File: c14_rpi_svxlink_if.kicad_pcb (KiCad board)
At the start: 2 copper layers, 87 x 56 mm, 52 parts, among them J1 RPi_GPIO, J2 Conn_01x04, J3 Conn_01x04, J4 Conn_01x04, J5 Conn_01x02, J6 Conn_01x04, J7 DB9F, Q1 BC847, Q2 BC847, Q3 BC847, Q4 BC857, T1 1:1, T2 1:1, U1 TLP222A, U2 HCPL-B17, U3 ADS1115_Module

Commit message: Small preproduction changes
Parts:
- C3: footprint Capacitor_THT:C_Rect_L7.2mm_W3.5mm_P5.00mm_FKS2_FKP2_MKS2_MKP2 -> Capacitor_THT:C_Rect_L7.2mm_W4.5mm_P5.00mm_FKS2_FKP2_MKS2_MKP2
- D3: value 18V -> TVS 18V
- J1: value RPi_GPIO -> RPi_GPIO Tall
- U1: value TLP222A -> TLP222A o. AQY282EH
- moved R18 16.9 mm to (198.8, 91.1)
- moved C6 16.8 mm to (196.1, 91.0)
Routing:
- net /RSSI: track 34.8 -> 17.7 mm
- net Net-(C6-Pad2): track 6.03 -> 16.4 mm
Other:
- board text added: "DL1COM C14 RPI SVXLINK IF v1.0"
- board text removed: "C14 RPI SVXLINK IF v1.0"

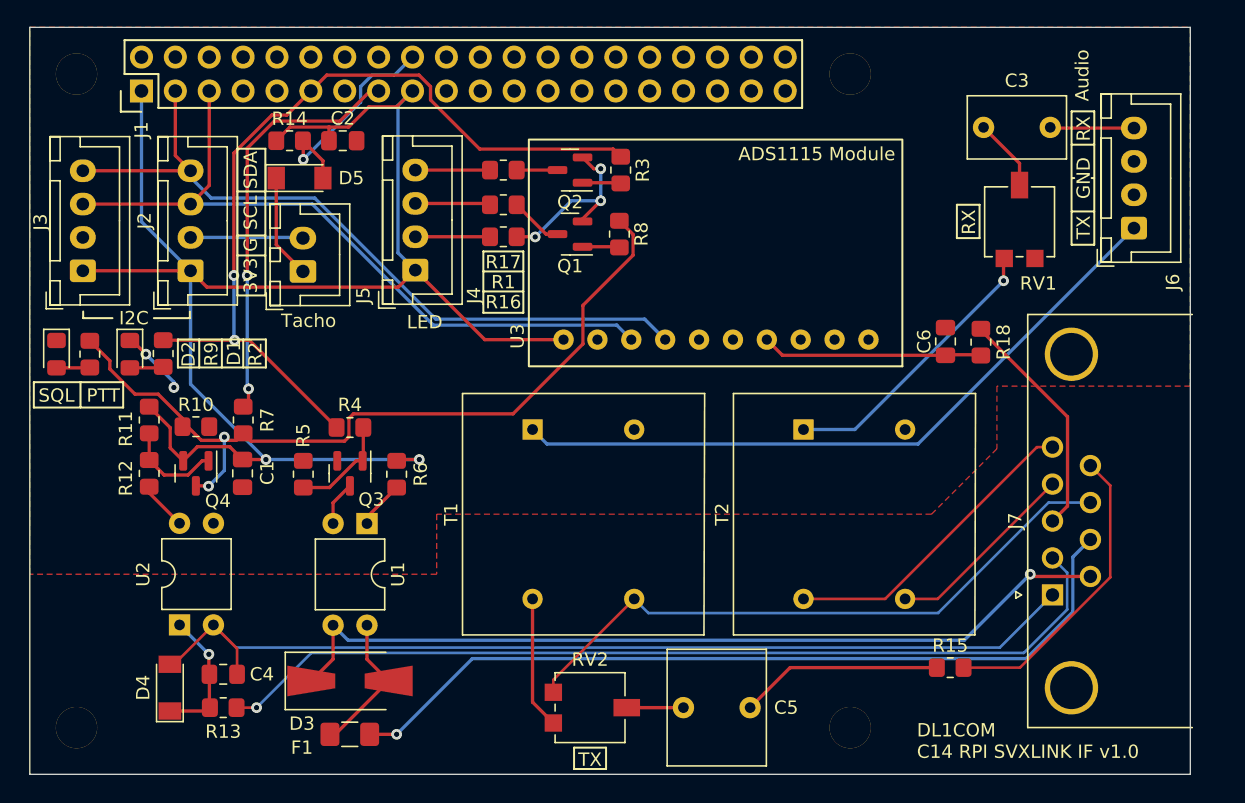
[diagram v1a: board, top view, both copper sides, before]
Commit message: Fix: Correct Footprint for J7 (M->F)
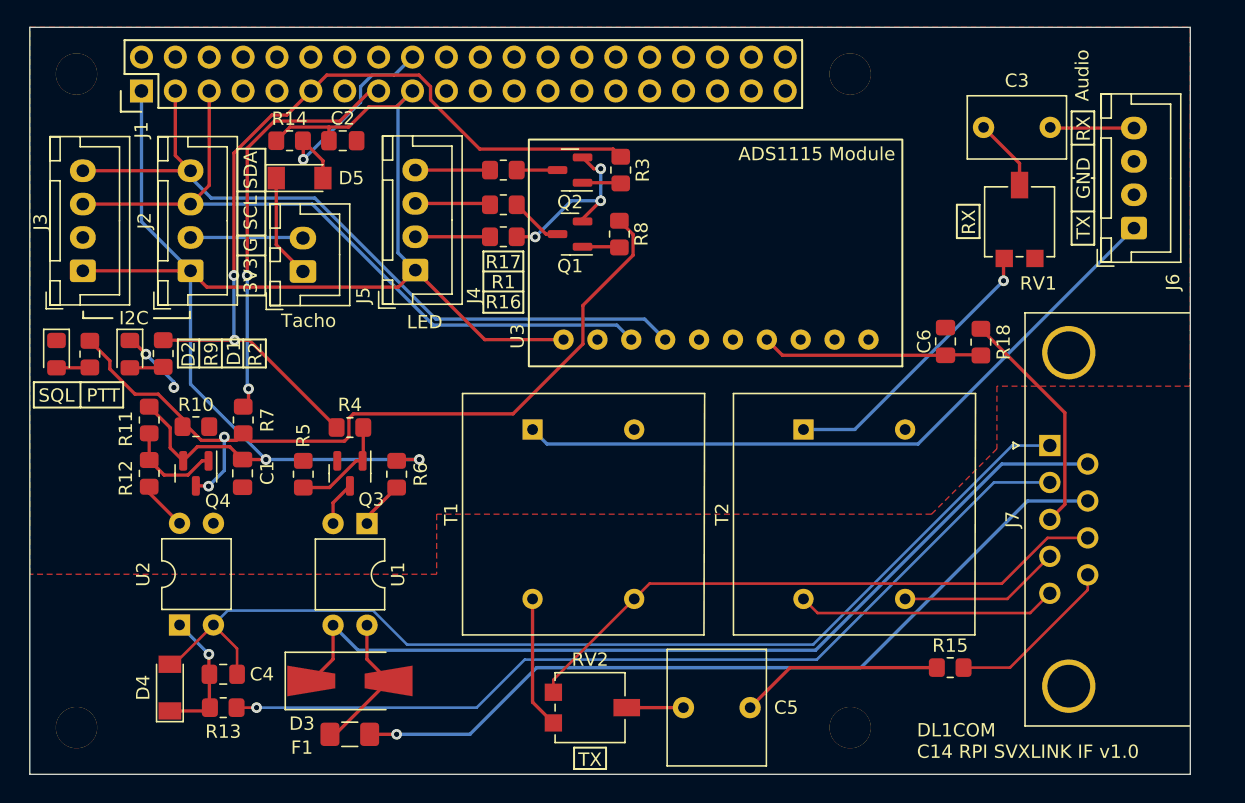
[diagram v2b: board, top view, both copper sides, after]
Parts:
- J7: footprint Connector_Dsub:DSUB-9_Male_Horizontal_P2.77x2.84mm_EdgePinOffset7.70mm_Housed_MountingHolesOffset9.12mm -> Connector_Dsub:DSUB-9_Female_Horizontal_P2.77x2.84mm_EdgePinOffset7.70mm_Housed_MountingHolesOffset9.12mm
- moved J7 11.2 mm to (204.0, 98.8)
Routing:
- net /TX_AUDIO+: track 22.8 -> 12.9 mm
- net /SQL_DET-: track 74.2 -> 79.3 mm
- net /RX_AUDIO+: track 23.4 -> 19.5 mm
- net /PTT_GND: track 64.2 -> 68.0 mm, vias 1 -> 0
- net /RX_AUDIO-: track 14.6 -> 12.2 mm
- net /TX_AUDIO-: track 47.6 -> 45.4 mm
- net /SQL_DET+: track 69.6 -> 68.0 mm
- net /PTT+: track 62.5 -> 61.1 mm

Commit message: Added Fiducials
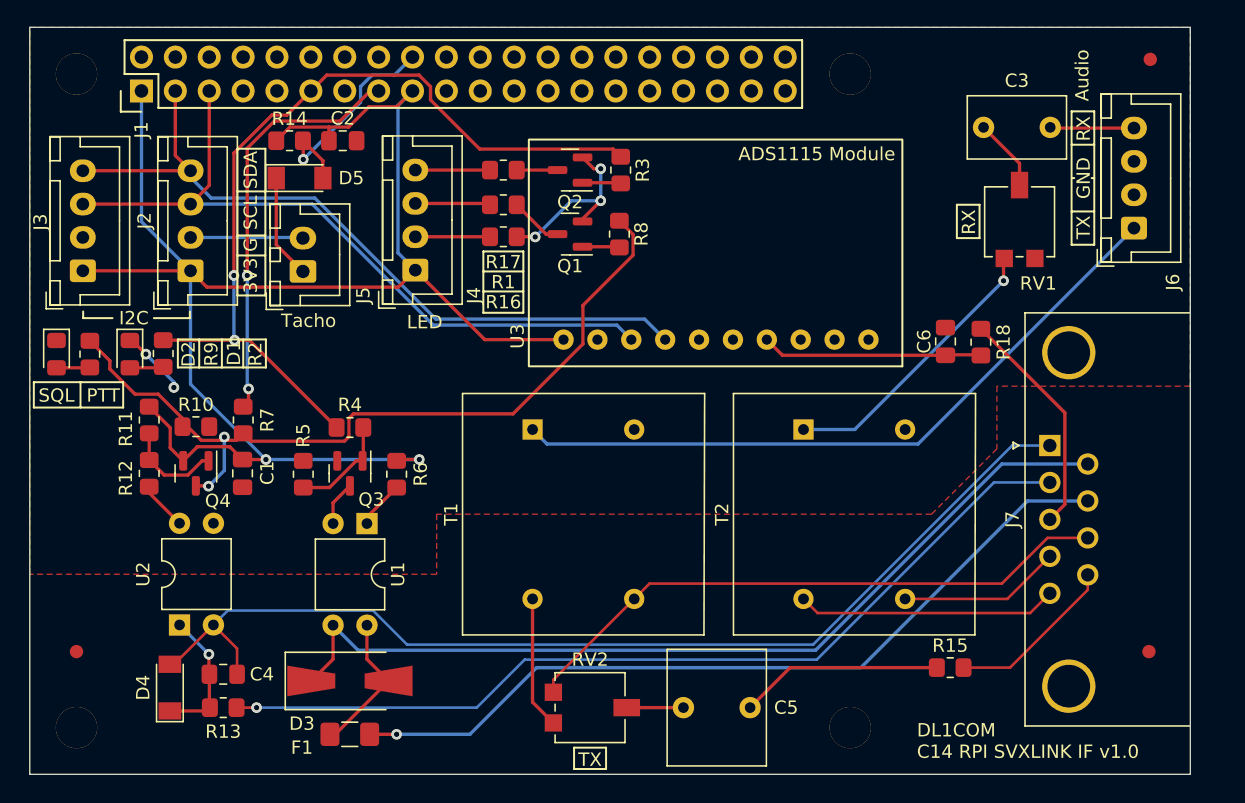
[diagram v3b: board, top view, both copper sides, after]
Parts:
- added REF**: Fiducial_1mm_Mask3mm, Fiducial:Fiducial_1mm_Mask3mm, F.Cu at (211.4, 114.3)
- added REF**: Fiducial_1mm_Mask3mm, Fiducial:Fiducial_1mm_Mask3mm, F.Cu at (131.0, 114.3)
- added REF**: Fiducial_1mm_Mask3mm, Fiducial:Fiducial_1mm_Mask3mm, F.Cu at (211.5, 69.9)
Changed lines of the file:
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@@
     )
+  )
+  (footprint "Fiducial:Fiducial_1mm_Mask3mm" (layer "F.Cu")
+    (at 211.4 114.3)
+    (descr "Circular Fiducial, 1mm bare copper, 3mm soldermask opening (recommended)")
+    (tags "fiducial")
+    (attr smd)
+    (fp_text reference "REF**" (at 0 -2.54) (layer "F.SilkS") hide
+      (effects (font (size 1 1) (thickness 0.15)))
+    )
+    (fp_text value "Fiducial_1mm_Mask3mm" (at 0 2.286) (layer "F.Fab")
+      (effects (font (size 1 1) (thickness 0.15)))
+    )
+    (fp_text user "${REFERENCE}" (at 0 0) (layer "F.Fab")
+      (effects (font (size 0.4 0.4) (thickness 0.06)))
+    )
+    (fp_circle (center 0 0) (end 1.75 0) (layer "F.CrtYd") (width 0.05) (fill none))
+    (fp_circle (center 0 0) (end 1.5 0) (layer "F.Fab") (width 0.1) (fill none))
+    (pad "" smd circle locked (at 0 0) (size 1 1) (layers "F.Cu" "F.Mask")
+      (solder_mask_margin 1) (clearance 1))
   )
   (footprint "Resistor_SMD:R_0805_2012Metric_Pad1.20x1.40mm_HandSolder" (layer "F.Cu")
@@
       (rotate (xyz 0 0 0))
     )
+  )
+  (footprint "Fiducial:Fiducial_1mm_Mask3mm" (layer "F.Cu")
+    (at 131 114.3)
+    (descr "Circular Fiducial, 1mm bare copper, 3mm soldermask opening (recommended)")
+    (tags "fiducial")
+    (attr smd)
+    (fp_text reference "REF**" (at 0 -2.54) (layer "F.SilkS") hide
+      (effects (font (size 1 1) (thickness 0.15)))
+    )
+    (fp_text value "Fiducial_1mm_Mask3mm" (at 0 2.286) (layer "F.Fab")
+      (effects (font (size 1 1) (thickness 0.15)))
+    )
+    (fp_text user "${REFERENCE}" (at 0 0) (layer "F.Fab")
+      (effects (font (size 0.4 0.4) (thickness 0.06)))
+    )
+    (fp_circle (center 0 0) (end 1.75 0) (layer "F.CrtYd") (width 0.05) (fill none))
+    (fp_circle (center 0 0) (end 1.5 0) (layer "F.Fab") (width 0.1) (fill none))
+    (pad "" smd circle locked (at 0 0) (size 1 1) (layers "F.Cu" "F.Mask")
+      (solder_mask_margin 1) (clearance 1))
   )
   (footprint "RPi_Hat:RPi_Hat_Mounting_Hole" (layer "F.Cu")
@@
     )
   )
+  (footprint "Fiducial:Fiducial_1mm_Mask3mm" (layer "F.Cu")
+    (at 211.5 69.9)
+    (descr "Circular Fiducial, 1mm bare copper, 3mm soldermask opening (recommended)")
+    (tags "fiducial")
+    (attr smd)
+    (fp_text reference "REF**" (at 0 -2.54) (layer "F.SilkS") hide
+      (effects (font (size 1 1) (thickness 0.15)))
+    )
+    (fp_text value "Fiducial_1mm_Mask3mm" (at 0 2.286) (layer "F.Fab")
+      (effects (font (size 1 1) (thickness 0.15)))
+    )
+    (fp_text user "${REFERENCE}" (at 0 0) (layer "F.Fab")
+      (effects (font (size 0.4 0.4) (thickness 0.06)))
+    )
+    (fp_circle (center 0 0) (end 1.75 0) (layer "F.CrtYd") (width 0.05) (fill none))
+    (fp_circle (center 0 0) (end 1.5 0) (layer "F.Fab") (width 0.1) (fill none))
+    (pad "" smd circle locked (at 0 0) (size 1 1) (layers "F.Cu" "F.Mask")
+      (solder_mask_margin 1) (clearance 1))
+  )
   (footprint "LED_SMD:LED_0805_2012Metric_Pad1.15x1.40mm_HandSolder" (layer "F.Cu")

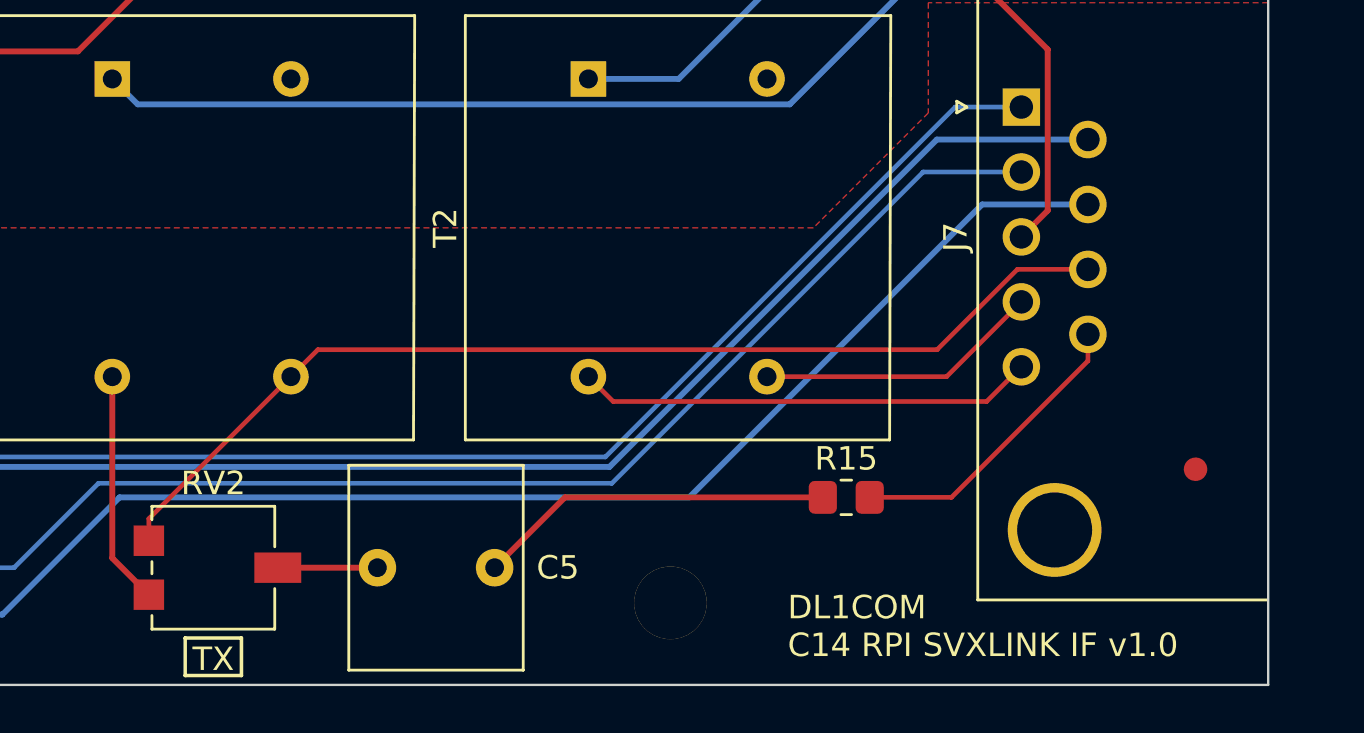
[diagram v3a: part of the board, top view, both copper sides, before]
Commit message: Add License and OSHW logo
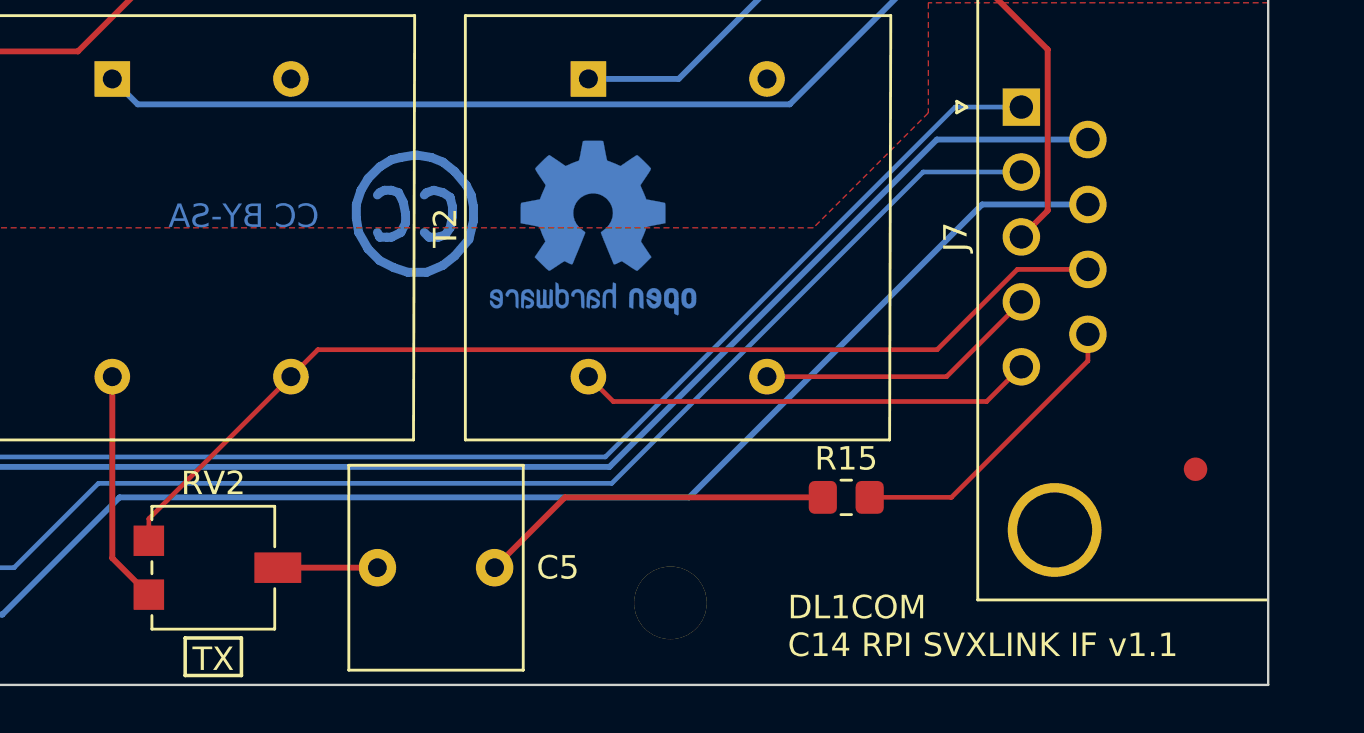
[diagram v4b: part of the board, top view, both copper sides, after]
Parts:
- added REF**: Symbol_CreativeCommons_CopperTop_Type2_Small, Symbol:Symbol_CreativeCommons_CopperTop_Type2_Small, B.Cu at (178.2, 103.5)
- added REF**: OSHW-Logo2_9.8x8mm_Copper, Symbol:OSHW-Logo2_9.8x8mm_Copper, B.Cu at (185.7, 104.0)
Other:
- board text added: "CC BY-SA"
- board text added: "DL1COM C14 RPI SVXLINK IF v1.1"
- board text removed: "DL1COM C14 RPI SVXLINK IF v1.0"

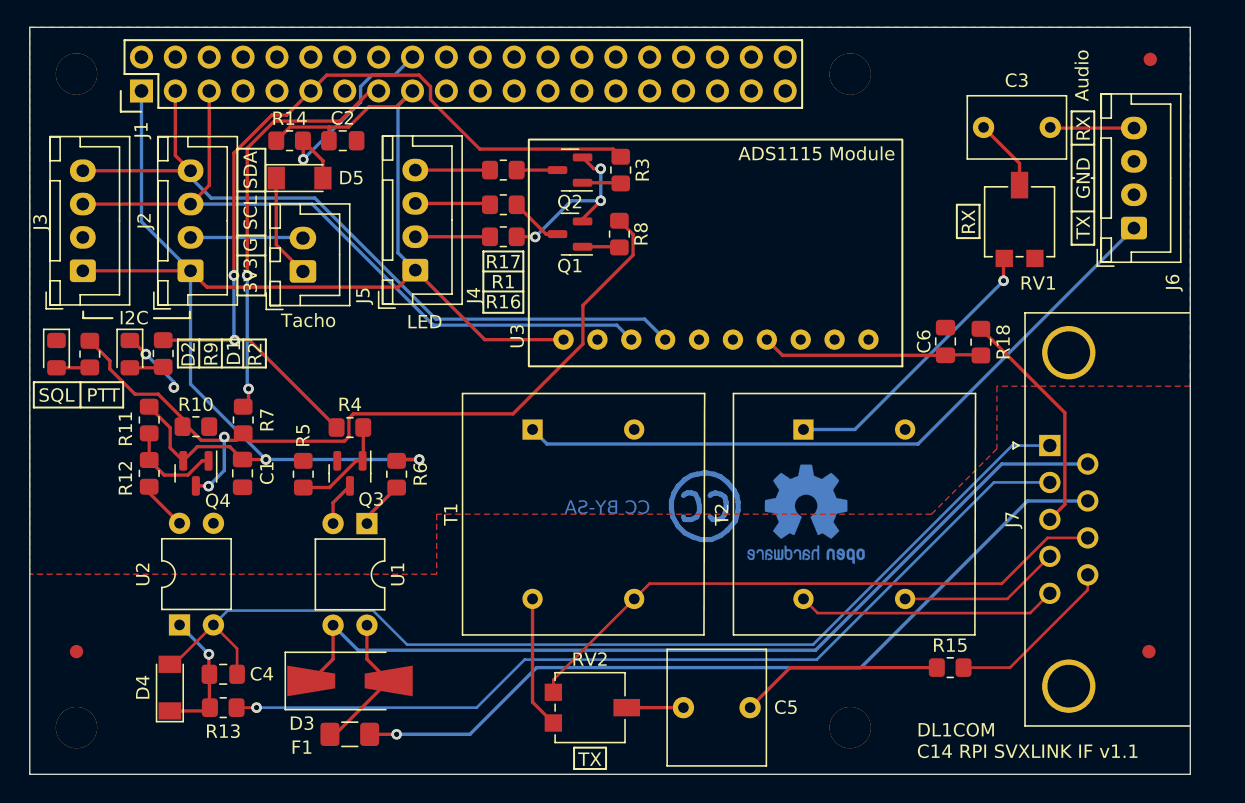
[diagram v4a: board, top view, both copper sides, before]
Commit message: Add Open Collector for Fan Ctrl
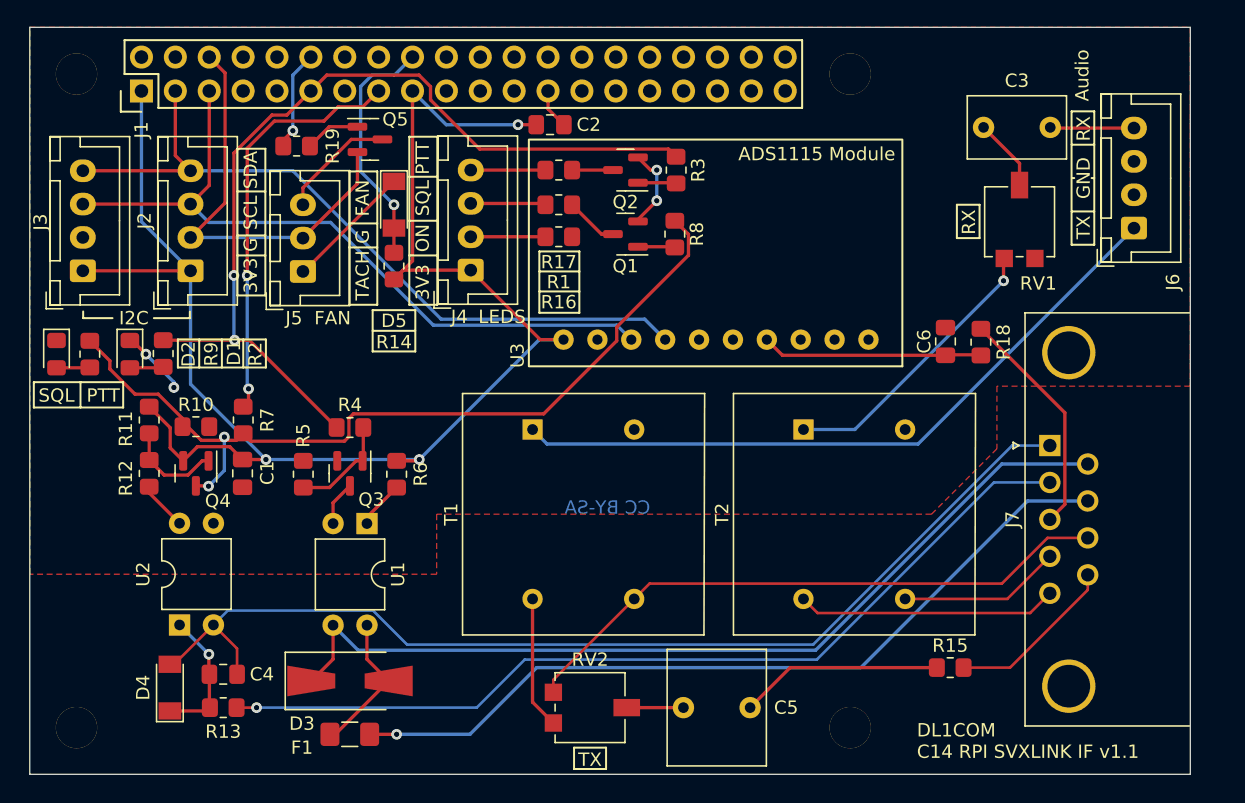
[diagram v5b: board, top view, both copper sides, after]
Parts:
- removed REF** (x3): Fiducial_1mm_Mask3mm, Fiducial:Fiducial_1mm_Mask3mm
- removed REF**: Symbol_CreativeCommons_CopperTop_Type2_Small, Symbol:Symbol_CreativeCommons_CopperTop_Type2_Small
- removed REF**: OSHW-Logo2_9.8x8mm_Copper, Symbol:OSHW-Logo2_9.8x8mm_Copper
- added Q5: BC847, Package_TO_SOT_SMD:SOT-23, F.Cu at (153.0, 75.9)
- added R19: 22k, Resistor_SMD:R_0805_2012Metric_Pad1.20x1.40mm_HandSolder, F.Cu at (147.5, 76.4)
- J5: footprint Connector_JST:JST_XH_B2B-XH-A_1x02_P2.50mm_Vertical -> Connector_JST:JST_XH_B3B-XH-A_1x03_P2.50mm_Vertical
- moved C2 15.6 mm to (166.5, 74.8)
- moved R14 12.2 mm to (154.8, 85.4), turned to 90 degrees
- moved D5 7.35 mm to (154.8, 80.8), turned to -90 degrees
- moved R8 4.15 mm to (175.9, 83.0)
- moved J4 4.15 mm to (160.6, 85.7)
- moved Q1 4.15 mm to (172.2, 83.0)
- moved Q2 4.15 mm to (172.2, 78.2)
- moved R1 4.15 mm to (167.2, 80.8)
- moved R16 4.15 mm to (167.2, 83.2)
- moved R17 4.15 mm to (167.2, 78.2)
- moved R3 4.15 mm to (176.0, 78.2)
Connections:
- J1 pad 12: unconnected-(J1-Pad12) -> /RPI_FAN_CTRL
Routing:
- net GND: track 27.4 -> 46.2 mm, vias 5 -> 4
- net Net-(J5-Pad3): track 0.00 -> 8.74 mm
- net /RPI_FAN_CTRL: track 0.00 -> 7.53 mm, vias 0 -> 1
- net Net-(Q5-Pad1): track 0.00 -> 4.16 mm
- net /RPI_PTT: track 64.3 -> 68.5 mm
- net +3V3: track 123.3 -> 119.7 mm, vias 2 -> 3
- net Net-(Q4-Pad3): track 61.4 -> 64.5 mm
- net Net-(D5-Pad1): track 7.83 -> 9.62 mm
- net /RPI_FAN_TACHO: track 16.9 -> 18.3 mm
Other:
- board text added: "FAN"
- board text added: "LEDS"
- board text added: "ON"
- board text added: "RPi GPIO17 (pin 11) - PTT GPIO22 (pin 15) - SQL Det. GPIO18 (pin 12) - Fan Ctrl GPIO24 (pin 18) - Fan Tacho"
- board text added: "TACH"
- board text removed: "LED"
- board text removed: "RPi GPIO17 (pin 11) - PTT GPIO22 (pin 15) - SQL Det. GPIO24 (pin 18) - Fan Tacho"
- board text removed: "Tacho"
